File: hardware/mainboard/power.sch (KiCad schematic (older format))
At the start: 10 parts, among them U1 LM4040DBZ-10

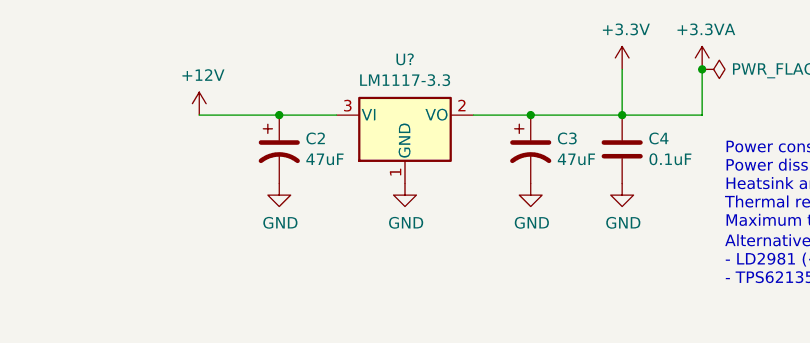
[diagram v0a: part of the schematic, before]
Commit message: start to change to tht!
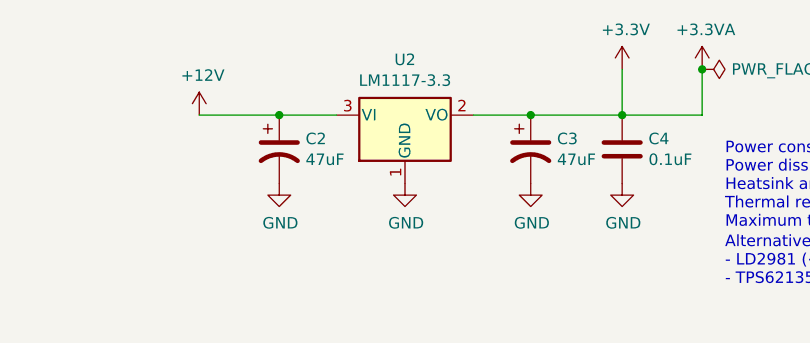
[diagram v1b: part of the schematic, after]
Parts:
- C1, C4: footprint Capacitor_SMD:C_0603_1608Metric_Pad1.05x0.95mm_HandSolder -> Sonosus:Capacitor_NonPolarizedSmall
- C2, C3: footprint Capacitor_SMD:CP_Elec_6.3x5.8 -> Sonosus:Capacitor_Polarized
- D1, D2: footprint Diode_SMD:D_SOD-123 -> Sonosus:Diode_DO-35
- R1: footprint Resistor_SMD:R_0603_1608Metric_Pad1.05x0.95mm_HandSolder -> Sonosus:Resistor
- gave numbers to parts that had none: 1
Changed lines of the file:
@@
 F 0 "D1" H 2250 1300 50  0000 C CNN
 F 1 "1N5817" H 2250 1200 50  0000 C CNN
-F 2 "Diode_SMD:D_SOD-123" H 2250 1100 50  0001 C CNN
+F 2 "Sonosus:Diode_DO-35" H 2250 1100 50  0001 C CNN
 F 3 "~" H 2250 1100 50  0001 C CNN
 F 4 "yes" H 2250 1100 50  0001 C CNN "finalized"
@@
 F 0 "D2" H 2250 1550 50  0000 C CNN
 F 1 "1N5817" H 2250 1650 50  0000 C CNN
-F 2 "Diode_SMD:D_SOD-123" H 2250 1750 50  0001 C CNN
+F 2 "Sonosus:Diode_DO-35" H 2250 1750 50  0001 C CNN
 F 3 "~" H 2250 1750 50  0001 C CNN
 F 4 "yes" H 2250 1750 50  0001 C CNN "finalized"
@@
 F 0 "C3" H 5315 1396 50  0000 L CNN
 F 1 "47uF" H 5315 1305 50  0000 L CNN
-F 2 "Capacitor_SMD:CP_Elec_6.3x5.8" H 5200 1350 50  0001 C CNN
+F 2 "Sonosus:Capacitor_Polarized" H 5200 1350 50  0001 C CNN
 F 3 "~" H 5200 1350 50  0001 C CNN
 F 4 "ESR 0.3-22 Ohms, 16v+" H 5200 1350 50  0001 C CNN "Reqs"
@@
 F 0 "C4" H 5715 1396 50  0000 L CNN
 F 1 "0.1uF" H 5715 1305 50  0000 L CNN
-F 2 "Capacitor_SMD:C_0603_1608Metric_Pad1.05x0.95mm_HandSolder" H 5638 1200 50  0001 C CNN
+F 2 "Sonosus:Capacitor_NonPolarizedSmall" H 5638 1200 50  0001 C CNN
 F 3 "~" H 5600 1350 50  0001 C CNN
 F 4 "yes" H 5600 1350 50  0001 C CNN "finalized"
@@
 F 0 "C2" H 4215 1396 50  0000 L CNN
 F 1 "47uF" H 4215 1305 50  0000 L CNN
-F 2 "Capacitor_SMD:CP_Elec_6.3x5.8" H 4100 1350 50  0001 C CNN
+F 2 "Sonosus:Capacitor_Polarized" H 4100 1350 50  0001 C CNN
 F 3 "~" H 4100 1350 50  0001 C CNN
 F 4 "EEE-FK1V470P" H 4100 1350 50  0001 C CNN "mpn"
@@
 F 0 "R1" H 2268 2846 50  0000 L CNN
 F 1 "2.2k" H 2268 2755 50  0000 L CNN
-F 2 "Resistor_SMD:R_0603_1608Metric_Pad1.05x0.95mm_HandSolder" V 2240 2790 50  0001 C CNN
+F 2 "Sonosus:Resistor" V 2240 2790 50  0001 C CNN
 F 3 "~" H 2200 2800 50  0001 C CNN
 F 4 "yes" H 2200 2800 50  0001 C CNN "finalized"
@@
 F 0 "C1" H 2665 3346 50  0000 L CNN
 F 1 "0.1uF" H 2665 3255 50  0000 L CNN
-F 2 "Capacitor_SMD:C_0603_1608Metric_Pad1.05x0.95mm_HandSolder" H 2588 3150 50  0001 C CNN
+F 2 "Sonosus:Capacitor_NonPolarizedSmall" H 2588 3150 50  0001 C CNN
 F 3 "~" H 2550 3300 50  0001 C CNN
 F 4 "yes" H 2550 3300 50  0001 C CNN "finalized"
@@
 Connection ~ 5950 1000
 $Comp
-L Regulator_Linear:LM1117-3.3 U?
+L Regulator_Linear:LM1117-3.3 U2
 U 1 1 6119BE38
 P 4650 1200
-F 0 "U?" H 4650 1442 50  0000 C CNN
+F 0 "U2" H 4650 1442 50  0000 C CNN
 F 1 "LM1117-3.3" H 4650 1351 50  0000 C CNN
 F 2 "" H 4650 1200 50  0001 C CNN
